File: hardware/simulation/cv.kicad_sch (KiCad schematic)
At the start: 22 parts, among them U1 ${SIM.PARAMS}, U2 ${SIM.PARAMS}, U3 ${SIM.PARAMS}

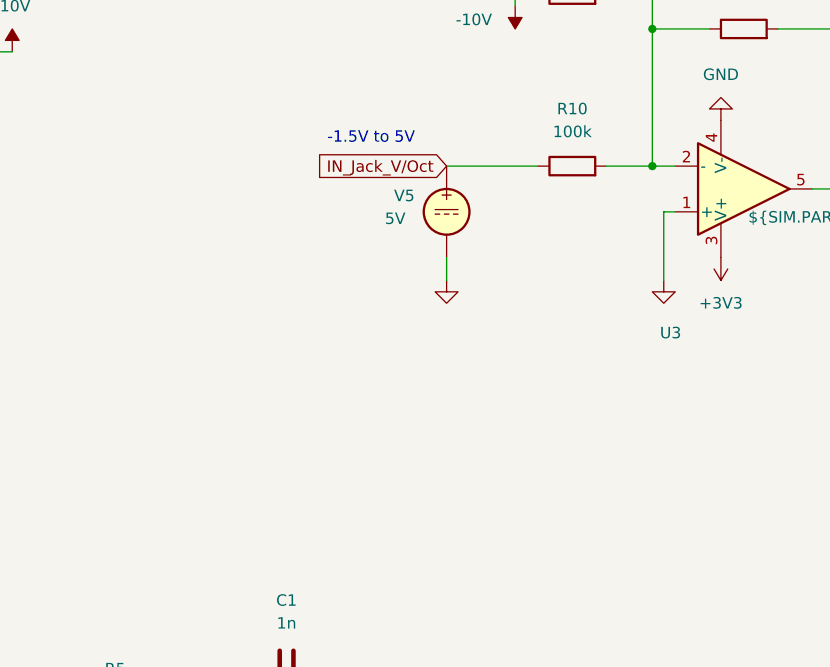
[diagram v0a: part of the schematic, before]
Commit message: feat: fixes in pcb design
- use correct BAT54S placement/layout
- fix pin mapping of fade potentiometers, also adjust routing
- switch pins that did not support PWM out (for fader led)
- switch pins that did not support EXTI
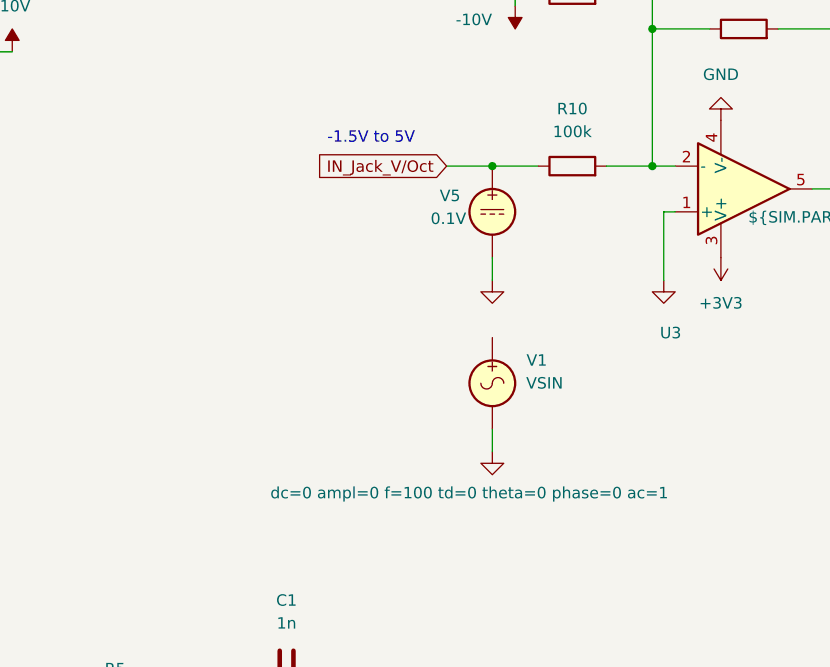
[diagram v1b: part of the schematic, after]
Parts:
- added V1: VSIN, symbol Simulation_SPICE:VSIN
- V5: value 5V -> 0.1V
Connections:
- net GND: now also V1.2
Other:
- moved on the sheet: V5
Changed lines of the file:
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@@
 	)
 	(junction
+		(at 105.41 69.85)
+		(diameter 0)
+		(color 0 0 0 0)
+	)
+	(junction
 		(at 123.19 50.8)
 		(diameter 0)
@@
 	(wire
 		(pts
-			(xy 100.33 80.01) (xy 100.33 82.55)
+			(xy 73.66 156.21) (xy 74.93 156.21)
 		)
 		(stroke
@@
 	(wire
 		(pts
-			(xy 73.66 156.21) (xy 74.93 156.21)
+			(xy 105.41 99.06) (xy 105.41 101.6)
 		)
 		(stroke
@@
 	(wire
 		(pts
+			(xy 105.41 80.01) (xy 105.41 82.55)
+		)
+		(stroke
+			(width 0)
+			(type default)
+		)
+	)
+	(wire
+		(pts
 			(xy 243.84 143.51) (xy 243.84 146.05)
 		)
@@
 	(wire
 		(pts
-			(xy 124.46 74.93) (xy 125.73 74.93)
+			(xy 105.41 69.85) (xy 110.49 69.85)
 		)
 		(stroke
@@
 	(wire
 		(pts
-			(xy 173.99 140.97) (xy 179.07 140.97)
+			(xy 124.46 74.93) (xy 125.73 74.93)
 		)
 		(stroke
@@
 	(wire
 		(pts
-			(xy 39.37 57.15) (xy 52.07 57.15)
+			(xy 173.99 140.97) (xy 179.07 140.97)
 		)
 		(stroke
@@
 	(wire
 		(pts
-			(xy 123.19 44.45) (xy 123.19 50.8)
+			(xy 39.37 57.15) (xy 52.07 57.15)
 		)
 		(stroke
@@
 	(wire
 		(pts
-			(xy 129.54 44.45) (xy 123.19 44.45)
+			(xy 123.19 44.45) (xy 123.19 50.8)
 		)
 		(stroke
@@
 	(wire
 		(pts
-			(xy 100.33 69.85) (xy 110.49 69.85)
+			(xy 129.54 44.45) (xy 123.19 44.45)
 		)
 		(stroke
@@
 	(wire
 		(pts
+			(xy 100.33 69.85) (xy 105.41 69.85)
+		)
+		(stroke
+			(width 0)
+			(type default)
+		)
+	)
+	(wire
+		(pts
 			(xy 195.58 151.13) (xy 195.58 153.67)
 		)
@@
 	(symbol
 		(lib_id "Simulation_SPICE:VDC")
-		(at 100.33 74.93 0)
+		(at 105.41 74.93 0)
 		(unit 1)
 		(exclude_from_sim no)
@@
 		(dnp no)
 		(property "Reference" "V5"
-			(at 94.488 73.152 0)
+			(at 99.568 73.152 0)
 			(effects
 				(font
@@
 			)
 		)
-		(property "Value" "5V"
-			(at 93.472 75.692 0)
+		(property "Value" "0.1V"
+			(at 98.552 75.692 0)
 			(effects
 				(font
@@
 		)
 		(property "Footprint" ""
-			(at 100.33 74.93 0)
+			(at 105.41 74.93 0)
 			(effects
 				(font
@@
 		)
 		(property "Datasheet" "https://ngspice.sourceforge.io/docs/ngspice-html-manual/manual.xhtml#sec_Independent_Sources_for"
-			(at 100.33 74.93 0)
+			(at 105.41 74.93 0)
 			(effects
 				(font
@@
 		)
 		(property "Description" "Voltage source, DC"
-			(at 100.33 74.93 0)
+			(at 105.41 74.93 0)
 			(effects
 				(font
@@
 		)
 		(property "Sim.Pins" "1=+ 2=-"
-			(at 100.33 74.93 0)
+			(at 105.41 74.93 0)
 			(effects
 				(font
@@
 		)
 		(property "Sim.Type" "DC"
-			(at 100.33 74.93 0)
+			(at 105.41 74.93 0)
 			(effects
 				(font
@@
 		)
 		(property "Sim.Device" "V"
-			(at 100.33 74.93 0)
+			(at 105.41 74.93 0)
 			(effects
 				(font
@@
 				)
 			)
-			(project "simulation"
-				(path "/e80dc9b1-658c-4466-ab44-cdfb41cf2b69/270709a9-ed21-4350-9ff3-4cd2d88db2d4"
-					(reference "V7")
-					(unit 1)
-				)
-			)
 		)
 	)
@@
 	)
 	(symbol
+		(lib_id "Simulation_SPICE:VSIN")
+		(at 105.41 93.98 0)
+		(mirror y)
+		(unit 1)
+		(exclude_from_sim no)
+		(in_bom no)
+		(on_board no)
+		(dnp no)
+		(property "Reference" "V1"
+			(at 111.506 91.44 0)
+			(effects
+				(font
+					(size 1.27 1.27)
+				)
+				(justify left)
+			)
+		)
+		(property "Value" "VSIN"
+			(at 113.284 93.98 0)
+			(effects
+				(font
+					(size 1.27 1.27)
+				)
+				(justify left)
+			)
+		)
+		(property "Footprint" ""
+			(at 105.41 93.98 0)
+			(effects
+				(font
+					(size 1.27 1.27)
+				)
+				(hide yes)
+			)
+		)
+		(property "Datasheet" "https://ngspice.sourceforge.io/docs/ngspice-html-manual/manual.xhtml#sec_Independent_Sources_for"
+			(at 105.41 93.98 0)
+			(effects
+				(font
+					(size 1.27 1.27)
+				)
+				(hide yes)
+			)
+		)
+		(property "Description" "Voltage source, sinusoidal"
+			(at 105.41 93.98 0)
+			(effects
+				(font
+					(size 1.27 1.27)
+				)
+				(hide yes)
+			)
+		)
+		(property "Sim.Pins" "1=+ 2=-"
+			(at 105.41 93.98 0)
+			(effects
+				(font
+					(size 1.27 1.27)
+				)
+				(hide yes)
+			)
+		)
+		(property "Sim.Params" "dc=0 ampl=0 f=100 td=0 theta=0 phase=0 ac=1"
+			(at 124.968 106.172 0)
+			(effects
+				(font
+					(size 1.27 1.27)
+				)
+				(justify left)
+			)
+		)
+		(property "Sim.Type" "SIN"
+			(at 105.41 93.98 0)
+			(effects
+				(font
+					(size 1.27 1.27)
+				)
+				(hide yes)
+			)
+		)
+		(property "Sim.Device" "V"
+			(at 105.41 93.98 0)
+			(effects
+				(font
+					(size 1.27 1.27)
+				)
+				(justify left)
+				(hide yes)
+			)
+		)
+		(pin "2"
+		)
+		(pin "1"
+		)
+		(instances
+			(project "cv"
+				(path "/ac5dd659-8174-4dce-b2bd-6ff63c727fa9"
+					(reference "V1")
+					(unit 1)
+				)
+			)
+		)
+	)
+	(symbol
 		(lib_id "Device:R")
 		(at 158.75 78.74 0)
@@
 	(symbol
 		(lib_id "power:GND")
-		(at 100.33 82.55 0)
+		(at 105.41 82.55 0)
 		(mirror y)
 		(unit 1)
@@
 		(dnp no)
 		(property "Reference" "#PWR0104"
-			(at 100.33 88.9 0)
+			(at 105.41 88.9 0)
 			(effects
 				(font
@@
 		)
 		(property "Value" "GND"
-			(at 100.33 86.614 0)
+			(at 105.41 86.614 0)
 			(effects
 				(font
@@
 		)
 		(property "Footprint" ""
-			(at 100.33 82.55 0)
+			(at 105.41 82.55 0)
 			(effects
 				(font
@@
 		)
 		(property "Datasheet" ""
-			(at 100.33 82.55 0)
+			(at 105.41 82.55 0)
 			(effects
 				(font
@@
 		)
 		(property "Description" "Power symbol creates a global label with name \"GND\" , ground"
-			(at 100.33 82.55 0)
+			(at 105.41 82.55 0)
 			(effects
 				(font
@@
 				)
 			)
-			(project "simulation"
-				(path "/e80dc9b1-658c-4466-ab44-cdfb41cf2b69/270709a9-ed21-4350-9ff3-4cd2d88db2d4"
-					(reference "#PWR018")
-					(unit 1)
-				)
-			)
 		)
 	)
@@
 					(unit 1)
 				)
+			)
+		)
+	)
+	(symbol
+		(lib_id "power:GND")
+		(at 105.41 101.6 0)
+		(mirror y)
+		(unit 1)
+		(exclude_from_sim no)
+		(in_bom yes)
+		(on_board yes)
+		(dnp no)
+		(property "Reference" "#PWR03"
+			(at 105.41 107.95 0)
+			(effects
+				(font
+					(size 1.27 1.27)
+				)
+				(hide yes)
+			)
+		)
+		(property "Value" "GND"
+			(at 105.41 105.664 0)
+			(effects
+				(font
+					(size 1.27 1.27)
+				)
+				(hide yes)
+			)
+		)
+		(property "Footprint" ""
+			(at 105.41 101.6 0)
+			(effects
+				(font
+					(size 1.27 1.27)
+				)
+				(hide yes)
+			)
+		)
+		(property "Datasheet" ""
+			(at 105.41 101.6 0)
+			(effects
+				(font
+					(size 1.27 1.27)
+				)
+				(hide yes)
+			)
+		)
+		(property "Description" "Power symbol creates a global label with name \"GND\" , ground"
+			(at 105.41 101.6 0)
+			(effects
+				(font
+					(size 1.27 1.27)
+				)
+				(hide yes)
+			)
+		)
+		(pin "1"
+		)
+		(instances
+			(project "cv"
+				(path "/ac5dd659-8174-4dce-b2bd-6ff63c727fa9"
+					(reference "#PWR03")
+					(unit 1)
+				)
